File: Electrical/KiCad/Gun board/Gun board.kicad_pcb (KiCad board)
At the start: 2 copper layers, 99.1 x 80 mm, 0 parts

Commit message: Started adding footprints to PCB
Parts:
- added BT1: Battery, Connector_JST:JST_PH_S2B-PH-K_1x02_P2.00mm_Horizontal, F.Cu at (191.8, 96.5)
- added C1: 10μF, Capacitor_SMD:CP_Elec_5x5.4, F.Cu at (153.7, 69.8)
- added C10: 1μF, Capacitor_SMD:CP_Elec_4x5.4, F.Cu at (137.2, 59.7)
- added C11: 47nF, Capacitor_SMD:C_0805_2012Metric, F.Cu at (346.4, 94.0)
- added C12: 220μF, Capacitor_SMD:CP_Elec_8x10.5, F.Cu at (180.3, 27.9)
- added C13: 10μF, Capacitor_SMD:CP_Elec_5x5.4, F.Cu at (148.6, 36.8)
- added C14: 33nF, Capacitor_SMD:C_0805_2012Metric, F.Cu at (367.1, 76.0)
- added C15: 10nF, Capacitor_SMD:C_0805_2012Metric, F.Cu at (377.6, 59.1)
- added C16: 100nF, Capacitor_SMD:C_0805_2012Metric, F.Cu at (358.1, 97.8)
- added C17: 100nF, Capacitor_SMD:C_0805_2012Metric, F.Cu at (359.9, 81.8)
- added C18: 4.7μF, Capacitor_SMD:CP_Elec_4x5.4, F.Cu at (163.8, 45.7)
- added C2: 4.7μF, Capacitor_SMD:CP_Elec_4x5.4, F.Cu at (182.9, 88.9)
- added C3: 22μF, Capacitor_SMD:CP_Elec_6.3x5.4, F.Cu at (165.1, 69.8)
- added C4: 10μF, Capacitor_SMD:CP_Elec_5x5.4, F.Cu at (138.4, 26.7)
- added C5: 4.7μF, Capacitor_SMD:CP_Elec_4x5.4, F.Cu at (182.9, 97.8)
- added C6: 100nF, Capacitor_SMD:C_0805_2012Metric, F.Cu at (375.9, 88.9)
- added C7: 100nF, Capacitor_SMD:C_0805_2012Metric, F.Cu at (365.0, 79.0)
- added C8: 4.7μF, Capacitor_SMD:CP_Elec_4x5.4, F.Cu at (137.2, 52.1)
- added C9: 10nF, Capacitor_SMD:C_0805_2012Metric, F.Cu at (389.0, 66.0)
- added D1: MBR0520, Diode_SMD:D_SOD-123, F.Cu at (175.3, 97.8)
- added D2: LED, LED_THT:LED_D5.0mm, F.Cu at (108.0, 95.2)
- added D3: LED, LED_THT:LED_D5.0mm, F.Cu at (108.0, 30.5)
- added J2: Conn_01x05, Connector_PinHeader_2.54mm:PinHeader_1x05_P2.54mm_Vertical, F.Cu at (106.7, 55.9)
- added JP1: Jumper, Connector_PinHeader_2.54mm:PinHeader_1x02_P2.54mm_Vertical, F.Cu at (195.6, 48.3)
- added L1: 4.7μH, Inductor_SMD:L_10.4x10.4_H4.8, F.Cu at (194.3, 72.4)
- added LD1: Laserdiode_1C2A, Connector_JST:JST_PH_B2B-PH-K_1x02_P2.00mm_Vertical, F.Cu at (128.3, 96.5)
- added LD2: Laserdiode_1C2A, Connector_JST:JST_PH_B2B-PH-K_1x02_P2.00mm_Vertical, F.Cu at (137.2, 96.5)
- added LD3: Laserdiode_1C2A, Connector_JST:JST_PH_B2B-PH-K_1x02_P2.00mm_Vertical, F.Cu at (146.1, 96.5)
- added LD4: Laserdiode_1C2A, Connector_JST:JST_PH_B2B-PH-K_1x02_P2.00mm_Vertical, F.Cu at (154.9, 96.5)
- added LD5: Laserdiode_1C2A, Connector_JST:JST_PH_B2B-PH-K_1x02_P2.00mm_Vertical, F.Cu at (163.8, 96.5)
- added LS1: Speaker, Connector_JST:JST_PH_S2B-PH-K_1x02_P2.00mm_Horizontal, F.Cu at (191.8, 27.9)
- added Q1: 2N3904, Package_TO_SOT_THT:TO-92_Inline, F.Cu at (137.2, 73.7)
- added Q3: 2N3904, Package_TO_SOT_THT:TO-92_Inline, F.Cu at (106.7, 85.1)
- added Q4: 2N3904, Package_TO_SOT_THT:TO-92_Inline, F.Cu at (106.7, 45.7)
- added R1: 22Ω, Resistor_SMD:R_0805_2012Metric, F.Cu at (129.2, 90.2)
- added R10: 22Ω, Resistor_SMD:R_0805_2012Metric, F.Cu at (165.1, 90.2)
- added R11: 22Ω, Resistor_SMD:R_0805_2012Metric, F.Cu at (156.2, 90.2)
- added R12: 1MΩ, Resistor_SMD:R_0805_2012Metric, F.Cu at (175.3, 85.1)
- added R13: 330kΩ, Resistor_SMD:R_0805_2012Metric, F.Cu at (382.0, 62.0)
- added R14: 20kΩ, Resistor_SMD:R_0805_2012Metric, F.Cu at (371.5, 72.4)
- added R15: 10kΩ, Resistor_SMD:R_0805_2012Metric, F.Cu at (376.5, 66.6)
- added R16: 56Ω, Resistor_SMD:R_0805_2012Metric, F.Cu at (376.5, 69.6)
- added R17: 2kΩ, Resistor_SMD:R_0805_2012Metric, F.Cu at (370.8, 82.5)
- added R18: 10kΩ, Resistor_SMD:R_0805_2012Metric, F.Cu at (367.0, 94.0)
- added R19: 4.7kΩ, Resistor_SMD:R_0805_2012Metric, F.Cu at (383.5, 96.5)
- added R2: 1MΩ, Resistor_SMD:R_0805_2012Metric, F.Cu at (171.1, 90.2)
- added R20: 56Ω, Resistor_SMD:R_0805_2012Metric, F.Cu at (392.4, 74.9)
- added R26: 10Ω, Resistor_SMD:R_0805_2012Metric, F.Cu at (383.5, 81.3)
- added R3: 22Ω, Resistor_SMD:R_0805_2012Metric, F.Cu at (138.1, 90.2)
- added R4: 150kΩ, Resistor_SMD:R_0805_2012Metric, F.Cu at (143.2, 31.8)
- added R5: 22Ω, Resistor_SMD:R_0805_2012Metric, F.Cu at (147.0, 90.2)
- added R6: 20kΩ, Resistor_SMD:R_0805_2012Metric, F.Cu at (157.5, 29.2)
- added R7: 10kΩ, Resistor_SMD:R_0805_2012Metric, F.Cu at (157.1, 24.1)
- added R8: 4.7kΩ, Resistor_SMD:R_0805_2012Metric, F.Cu at (147.0, 48.3)
- added R9: 10kΩ, Resistor_SMD:R_0805_2012Metric, F.Cu at (144.4, 73.7)
- added SW1: SW_SPST, Connector_JST:JST_PH_S2B-PH-K_1x02_P2.00mm_Horizontal, F.Cu at (191.8, 85.1)
- added SW2: SW_SPST, Connector_JST:JST_PH_S2B-PH-K_1x02_P2.00mm_Horizontal, F.Cu at (191.8, 62.2)
- added U1: AAT1217, Package_TO_SOT_SMD:SOT-23-6, F.Cu at (175.3, 90.2)
- added U2: AMS1117, Package_TO_SOT_SMD:SOT-223-3_TabPin2, F.Cu at (167.6, 82.5)
- added U3: M25PX32-VMW, Package_SO:SOIJ-8_5.3x5.3mm_P1.27mm, F.Cu at (163.8, 55.9)
- added U4: MCP4725, Package_TO_SOT_SMD:SOT-23-6, F.Cu at (157.5, 40.6)
- added U5: STM32F030F4Px, Package_SO:TSSOP-20_4.4x6.5mm_P0.65mm, F.Cu at (147.3, 55.9)
- added U7: NRF24L01_Breakout, RF_Module:nRF24L01_Breakout, F.Cu at (116.8, 72.4)
- added U8: LM386, Package_SO:SOIC-8-1EP_3.9x4.9mm_P1.27mm_EP2.29x3mm, F.Cu at (148.6, 26.7)

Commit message: power and audio traces routed
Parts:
- added REF**: MountingHole_3.2mm_M3, MountingHole:MountingHole_3.2mm_M3, F.Cu at (171.2, 94.0)
- added REF**: MountingHole_3.2mm_M3, MountingHole:MountingHole_3.2mm_M3, F.Cu at (131.2, 94.0)
- C16, C17, C6, C7, C9, R1, R10, R11, R12, R13, R14, R16, R17, R19, R20, R3, R5, R8, R9: moved to B.Cu
- L1: footprint Inductor_SMD:L_10.4x10.4_H4.8 -> Inductor_SMD:L_TracoPower_TCK-141
- U8: footprint Package_SO:SOIC-8-1EP_3.9x4.9mm_P1.27mm_EP2.29x3mm -> Package_SO:SOIC-8_3.9x4.9mm_P1.27mm
- moved R20 281.3 mm to (113.0, 41.9), turned to 270 degrees
- moved R16 263.6 mm to (113.0, 77.5), turned to 270 degrees
- moved R15 249.7 mm to (127.0, 77.5), turned to 180 degrees
- moved R19 248.9 mm to (140.3, 43.8), turned to 180 degrees
- moved R18 248.0 mm to (127.0, 31.8), turned to 180 degrees
- moved C15 225.5 mm to (153.3, 35.6)
- moved C9 221.8 mm to (167.6, 50.8), turned to 90 degrees
- moved C6 215.3 mm to (163.8, 52.1)
- moved C16 214.8 mm to (151.1, 40.6)
- moved R26 208.0 mm to (180.3, 36.8)
- moved C7 203.3 mm to (163.8, 49.5), turned to 180 degrees
- moved C14 196.6 mm to (175.3, 33.0)
- moved R13 195.9 mm to (188.0, 88.9), turned to 270 degrees
- moved C17 195.1 mm to (166.4, 57.1), turned to 270 degrees
- moved R14 189.7 mm to (182.9, 92.7)
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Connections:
- U5 pad 19: /FLASH_CS -> /SYS_SWDIO
- U5 pad 20: /RADIO_CS -> /SYS_SWCLK
- U5 pad 8: Net-(U5-Pad8) -> /RADIO_CS
- U5 pad 9: Net-(U5-Pad9) -> /FLASH_CS
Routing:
- net GND: track 0.00 -> 89.2 mm, vias 0 -> 5
- net +5V: track 0.00 -> 40.5 mm, vias 0 -> 1
- net +BATT: track 0.00 -> 38.8 mm, vias 0 -> 1
- net Net-(C11-Pad1): track 0.00 -> 34.4 mm, vias 0 -> 2
- net Net-(C13-Pad1): track 0.00 -> 21.5 mm
- net Net-(BT1-Pad1): track 0.00 -> 17.2 mm
- net Net-(C13-Pad2): track 0.00 -> 16.9 mm
- net Net-(C4-Pad1): track 0.00 -> 14.8 mm
- net Net-(D1-Pad2): track 0.00 -> 14.3 mm
- net Net-(R13-Pad1): track 0.00 -> 14.1 mm, vias 0 -> 1
- net Net-(C14-Pad2): track 0.00 -> 12.1 mm
- net Net-(R4-Pad2): track 0.00 -> 11.9 mm
- net +3V3: track 0.00 -> 11.5 mm, vias 0 -> 1
- net Net-(C12-Pad2): track 0.00 -> 10.4 mm
- net Net-(C15-Pad2): track 0.00 -> 7.29 mm
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- added copper zone on B.Cu, net GND
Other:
- net class Signal added: clearance 0.2, trace_width 0.1524, via_dia 0.8, via_drill 0.4
- rule trace_min: 0.2 -> 0.127
- rule via_min_size: 0.4 -> 0.6
- board text added: "*"
- board text added: "Battery"
- board text added: "On/Off"
- board text added: "Speaker"
- board text added: "Trigger"

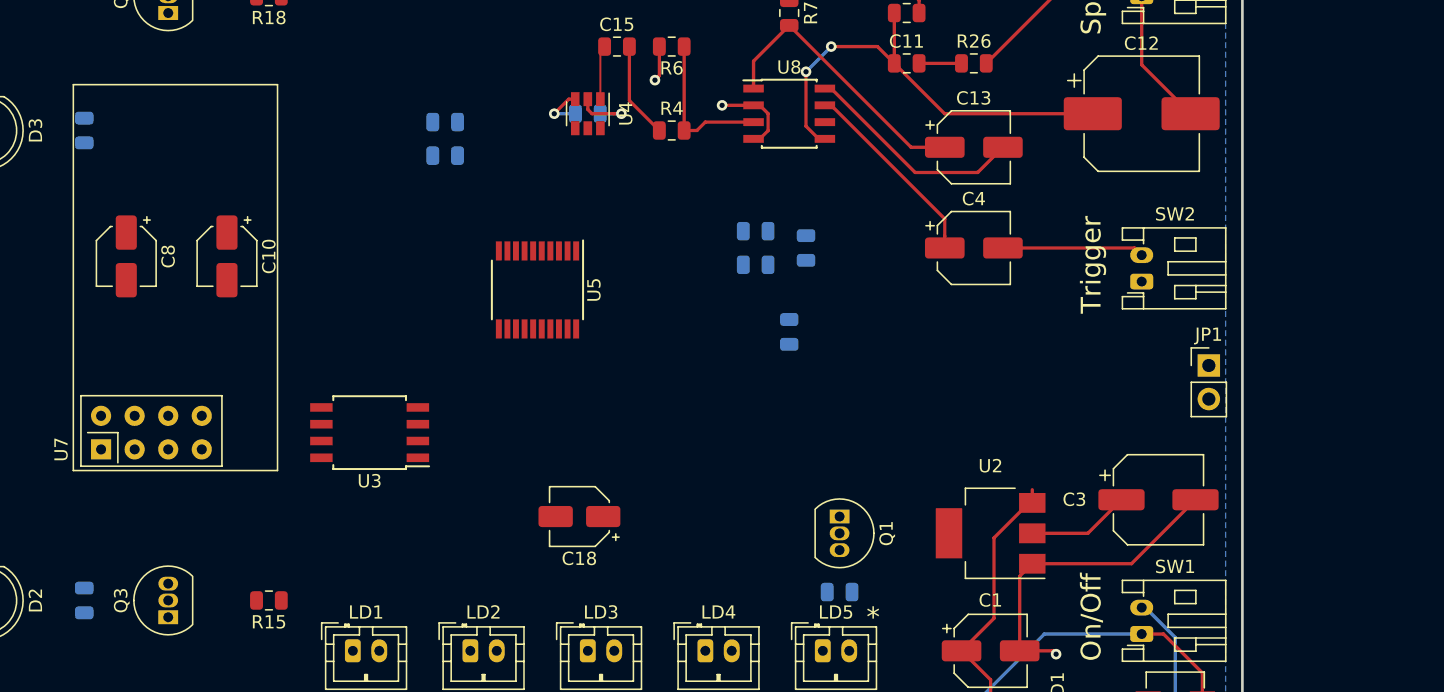
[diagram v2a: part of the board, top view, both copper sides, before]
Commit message: moved flash to backside of board
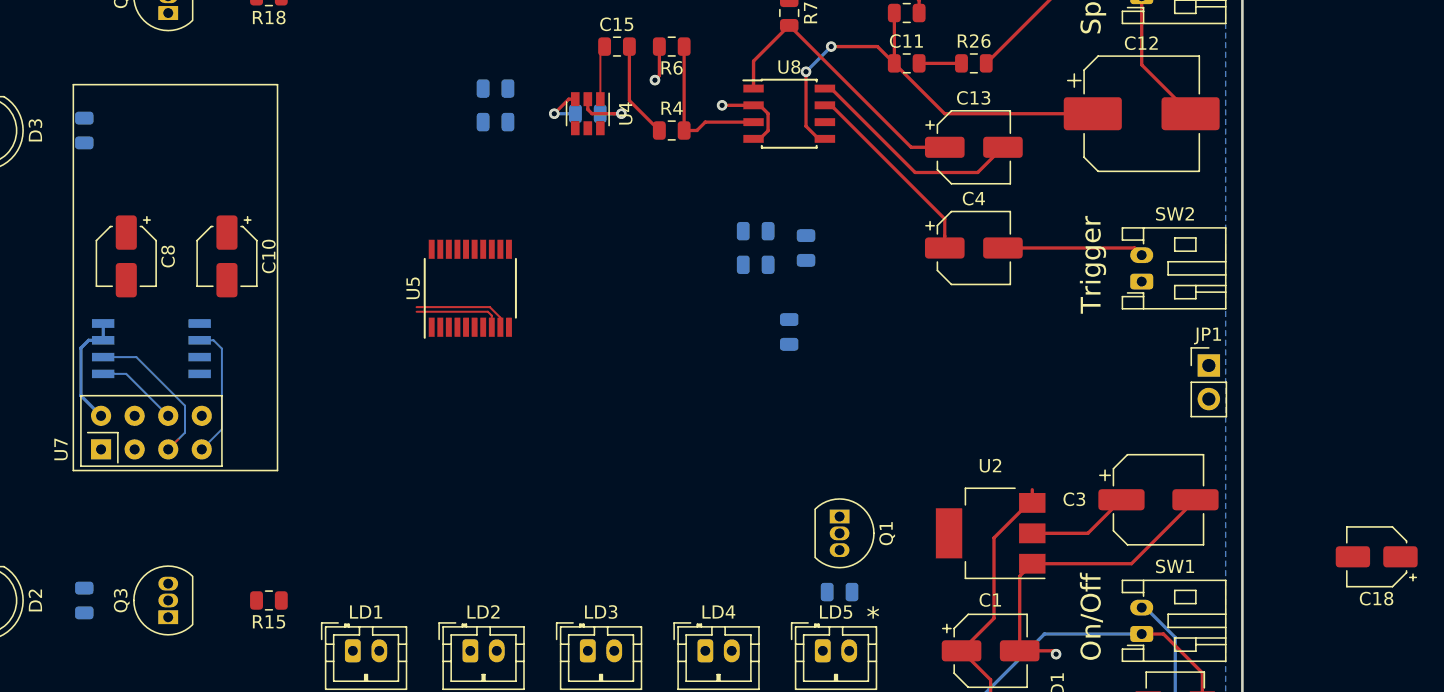
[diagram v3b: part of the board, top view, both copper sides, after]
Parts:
- U3: moved to B.Cu
- moved C18 60.4 mm to (210.8, 74.2)
- moved U3 17.7 mm to (118.1, 58.4)
- moved U5 5.08 mm to (142.2, 53.8), turned to 90 degrees
- moved R19 4.58 mm to (144.1, 41.3)
- moved R8 4.58 mm to (144.1, 38.7)
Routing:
- net /SCK: track 0.00 -> 12.6 mm
- net /MISO: track 0.00 -> 10.7 mm
- net +3V3: track 11.5 -> 20.4 mm
- net /FLASH_CS: track 0.00 -> 7.40 mm
- net /RADIO_CS: track 0.00 -> 6.69 mm
- net /MOSI: track 0.00 -> 6.24 mm

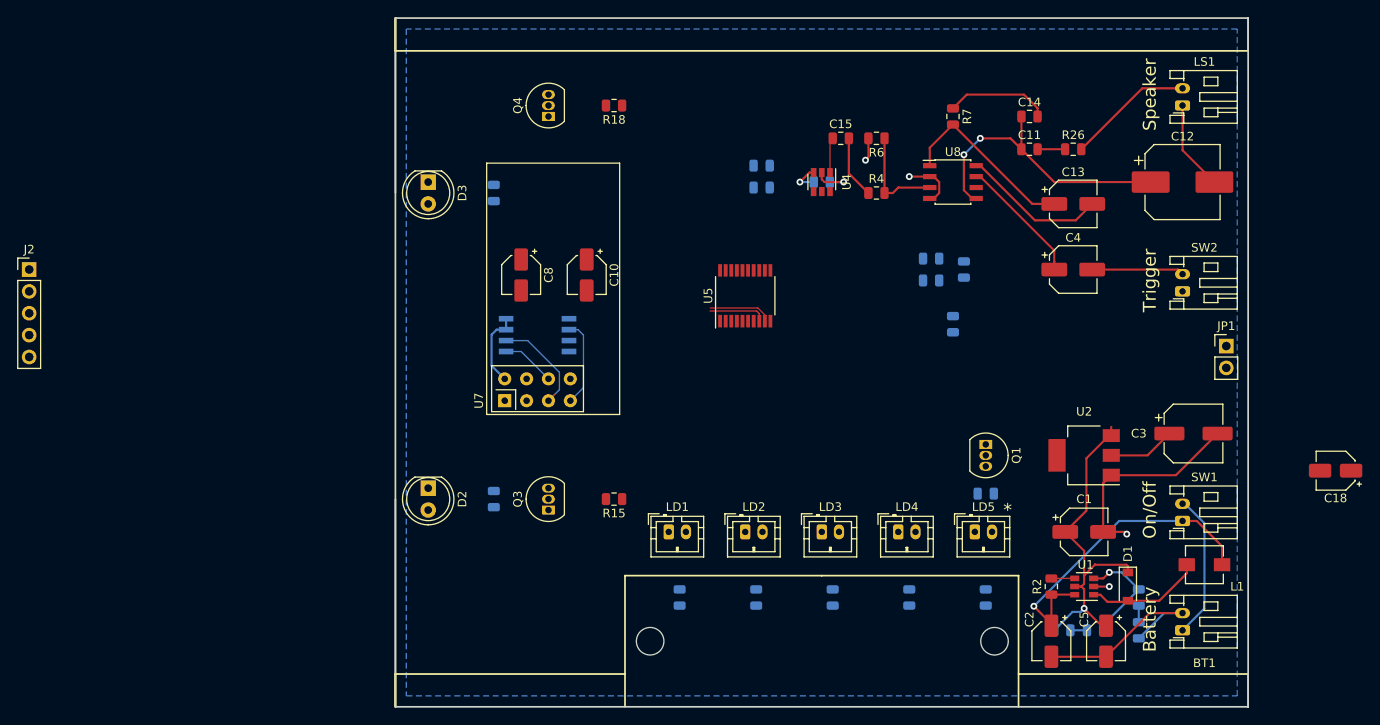
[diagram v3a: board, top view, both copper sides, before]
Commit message: Finished board layout, adding graphics
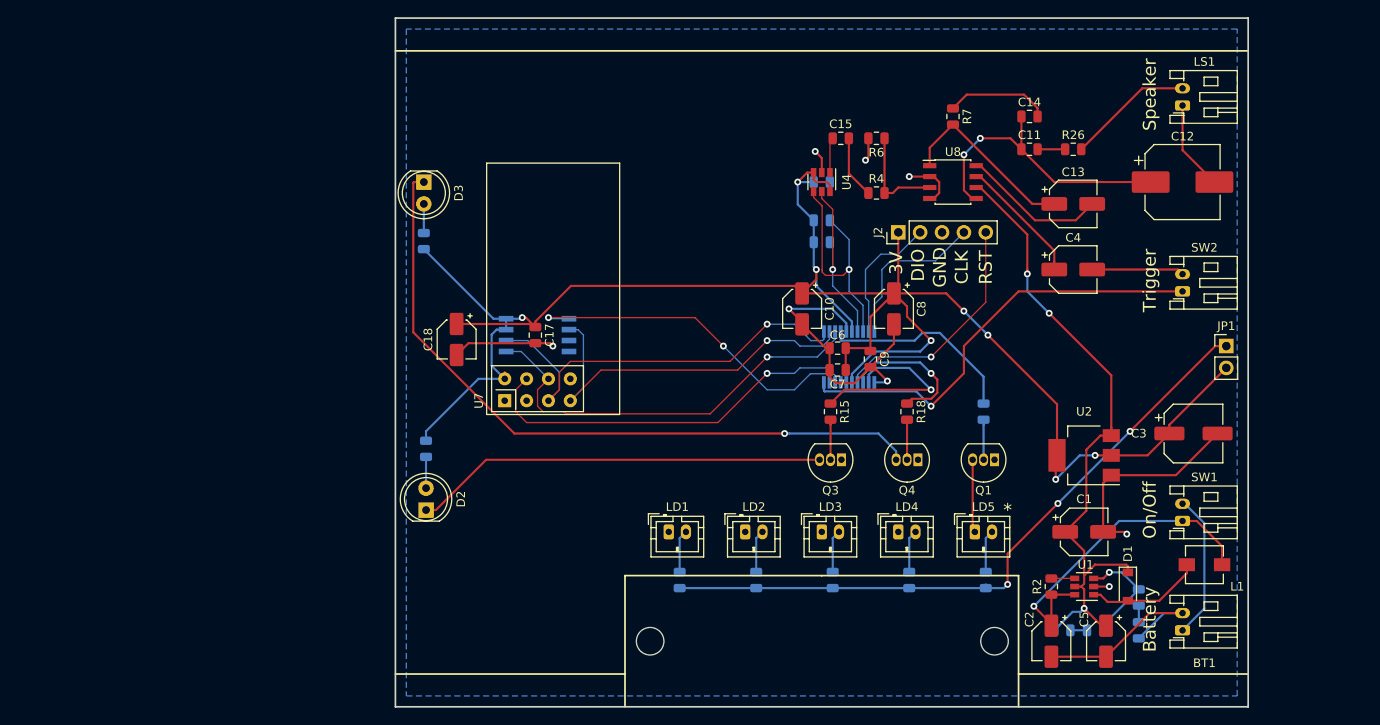
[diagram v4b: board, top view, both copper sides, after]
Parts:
- C17, C6, C7, C9: moved to F.Cu
- U5: moved to B.Cu
- moved C18 103.2 mm to (108.7, 58.9), turned to 270 degrees
- moved J2 101.1 mm to (160.0, 46.5), turned to 90 degrees
- moved Q4 58.6 mm to (162.3, 72.9), turned to 180 degrees
- moved R18 49.2 mm to (161.0, 67.3), turned to 270 degrees
- moved C17 48.5 mm to (117.9, 58.4)
- moved C8 43.5 mm to (159.5, 55.4)
- moved Q3 34.5 mm to (153.4, 72.9), turned to 180 degrees
- moved R15 27.1 mm to (152.1, 67.3), turned to 270 degrees
- moved C10 25.3 mm to (148.8, 55.4)
- moved C7 16.9 mm to (153.0, 62.5)
- moved C9 15.0 mm to (156.8, 61.2), turned to 270 degrees
- moved U5 14.0 mm to (154.3, 61.0)
- moved C6 13.4 mm to (153.0, 59.9), turned to 180 degrees
- moved R20 9.86 mm to (104.9, 47.5), turned to 90 degrees
- moved R16 9.80 mm to (105.2, 71.6)
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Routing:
- net +3V3: track 20.4 -> 222.9 mm, vias 1 -> 8
- net Net-(D3-Pad1): track 0.00 -> 81.4 mm, vias 0 -> 1
- net Net-(JP1-Pad1): track 0.00 -> 78.9 mm, vias 0 -> 3
- net /TRIGGER: track 0.00 -> 50.8 mm, vias 0 -> 1
- net Net-(D2-Pad1): track 0.00 -> 48.1 mm
- net GND: track 89.2 -> 133.7 mm, vias 5 -> 8
- net /MOSI: track 6.24 -> 49.3 mm, vias 0 -> 1
- net /RADIO_CS: track 6.69 -> 45.8 mm, vias 0 -> 1
- net /SCK: track 12.6 -> 50.2 mm, vias 0 -> 1
- net +5V: track 40.5 -> 76.5 mm, vias 1 -> 3
- net /MISO: track 10.7 -> 45.2 mm, vias 0 -> 1
- net /FLASH_CS: track 7.40 -> 40.4 mm, vias 0 -> 2
- net /RESET: track 0.00 -> 28.2 mm, vias 0 -> 1
- net /I2C_SDA: track 0.00 -> 27.9 mm, vias 0 -> 1
- net /STATUS: track 0.00 -> 23.2 mm
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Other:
- board text added: "3V"
- board text added: "CLK"
- board text added: "DIO"
- board text added: "GND"
- board text added: "RST"

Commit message: Added nameplate
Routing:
- added copper zone on F.Cu, net (none)

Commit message: added pcb info
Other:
- board text added: "Kitty Cosplay Reaper Costume Gun REV A01"
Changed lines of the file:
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@@
-(kicad_pcb (version 20171130) (host pcbnew "(5.1.0)-1")
+(kicad_pcb (version 20171130) (host pcbnew "(5.0.0)")
   (general
     (thickness 1.6)
-    (drawings 52)
+    (drawings 53)
     (tracks 445)
     (zones 0)
@@
     (zone_45_only no)
     (trace_min 0.127)
+    (segment_width 0.2)
+    (edge_width 0.15)
     (via_size 0.8)
     (via_drill 0.4)
@@
     (uvia_min_size 0.2)
     (uvia_min_drill 0.1)
-    (edge_width 0.15)
-    (segment_width 0.2)
     (pcb_text_width 0.3)
     (pcb_text_size 1.5 1.5)
@@
     (pad 1 np_thru_hole circle (at 0 0) (size 3.2 3.2) (drill 3.2) (layers *.Cu *.Mask))
   )
+  (gr_text "Kitty Cosplay\nReaper Costume Gun\n\nREV A01" (at 138.176 50.292 90) (layer F.SilkS)
+    (effects (font (size 1.5 1.5) (thickness 0.3)) (justify left))
+  )
   (gr_circle (center 123.698 86.487) (end 124.05721 86.487) (layer F.Mask) (width 0.2))

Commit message: Final Gerber files for manufacture
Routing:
- net Net-(R13-Pad1): track 14.1 -> 13.3 mm
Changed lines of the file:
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@@
     (thickness 1.6)
     (drawings 53)
-    (tracks 445)
+    (tracks 444)
     (zones 0)
     (modules 66)
@@
     (visible_elements 7FFFFFFF)
     (pcbplotparams
-      (layerselection 0x010fc_ffffffff)
+      (layerselection 0x010f0_ffffffff)
       (usegerberextensions false)
-      (usegerberattributes false)
+      (usegerberattributes true)
       (usegerberadvancedattributes false)
       (creategerberjobfile false)
-      (excludeedgelayer true)
+      (excludeedgelayer false)
       (linewidth 0.100000)
       (plotframeref false)
@@
       (outputformat 1)
       (mirror false)
-      (drillshape 1)
+      (drillshape 0)
       (scaleselection 1)
       (outputdirectory ""))
@@
   (segment (start 180.0075 92.71) (end 181.9425 92.71) (width 0.25) (layer B.Cu) (net 37))
   (via (at 184.531 85.979) (size 0.8) (drill 0.4) (layers F.Cu B.Cu) (net 38))
-  (segment (start 184.404 92.1235) (end 183.8175 92.71) (width 0.25) (layer B.Cu) (net 38))
   (segment (start 187.6275 87.63) (end 187.96 87.9625) (width 0.25) (layer B.Cu) (net 38))
   (segment (start 185.9765 85.979) (end 187.96 87.9625) (width 0.25) (layer B.Cu) (net 38))
